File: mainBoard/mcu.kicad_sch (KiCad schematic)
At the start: 25 parts, among them SW2 SW_SPDT, SW3 SW_Push, SW4 SW_Push, U4 STM32F401RETx, Y1 ATS240C-E

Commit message: Nearly finished with board after revisions
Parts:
- added TP17, TP18: TestPoint_Small, TestPoint:TestPoint_Pad_D1.0mm, symbol Connector:TestPoint_Small
- C14, C17, C20, C21, C22, C23, C24: Type (none) -> 50V X7R
- C15, C16: Type (none) -> 6.3V C0G; part number (none) -> 0402N200J500CT
- C18: value 2.2uF Low ESR -> 2.2uF; Type (none) -> 25V X7R; part number (none) -> CL21B225KAFNNNE
- C19: Type (none) -> 16V X7R
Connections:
- net HSE_IN: now also TP17.1
- net HSE_OUT: now also TP18.1
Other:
- note added: "CL21B225KAFNNNE"
- moved on the sheet: C15, C16, C18, C19, D14, D5, R10, R11, R58, R60, R9, SW2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

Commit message: work on AC power side
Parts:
- added TP19, TP20, TP21, TP22, TP23, TP24, TP25, TP26, TP27, TP28, TP29, TP30, TP31: TestPoint_Small, TestPoint:TestPoint_Pad_D1.0mm, symbol Connector:TestPoint_Small
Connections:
- net at U4.10 (PC2): now also TP21.1
- net at U4.11 (PC3): now also TP22.1
- net at U4.2 (PC13): now also TP24.1
- net at U4.21 (PA5): now also TP27.1
- net at U4.25 (PC5): now also TP23.1
- net at U4.26 (PB0): now also TP28.1
- net at U4.27 (PB1): now also TP29.1
- net at U4.28 (PB2): now also TP30.1
- net at U4.29 (PB10): now also TP31.1
- net at U4.3 (PC14): now also TP25.1
- net at U4.4 (PC15): now also TP26.1
- net at U4.8 (PC0): now also TP19.1
- net at U4.9 (PC1): now also TP20.1
- no-connect marks 13 -> 0

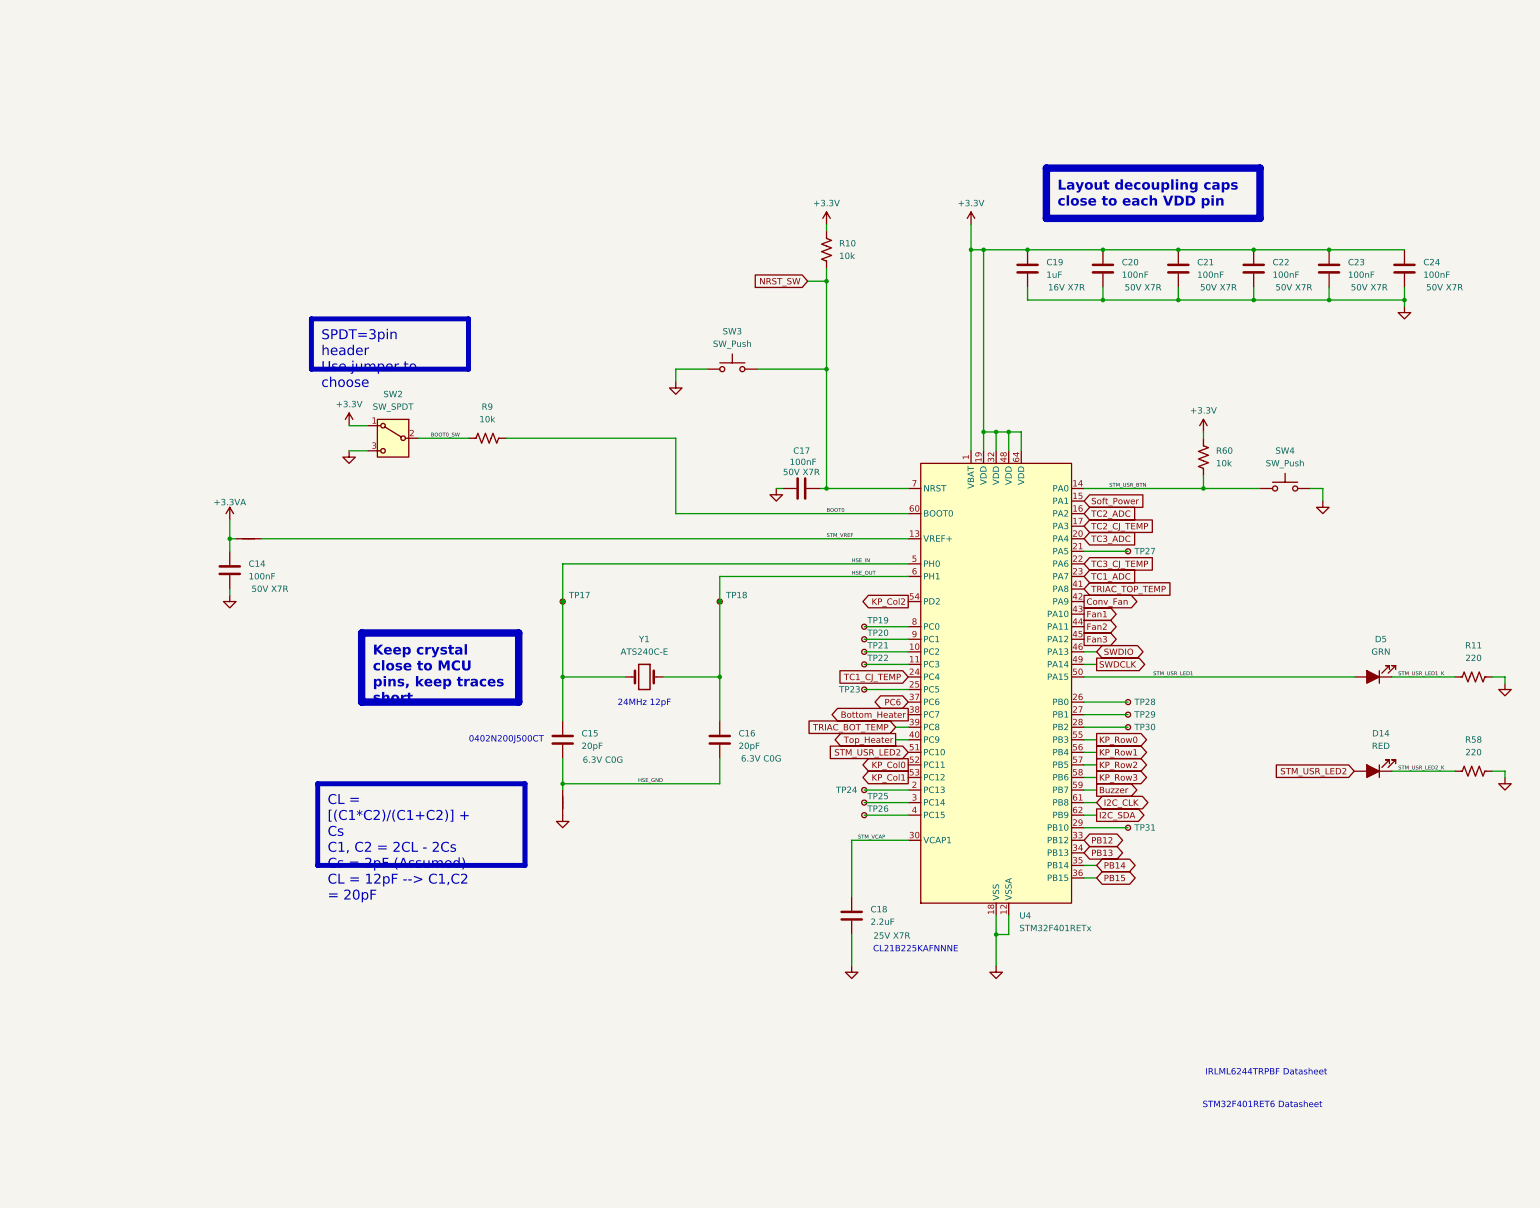
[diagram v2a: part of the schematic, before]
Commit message: add USB-A and change capacitors
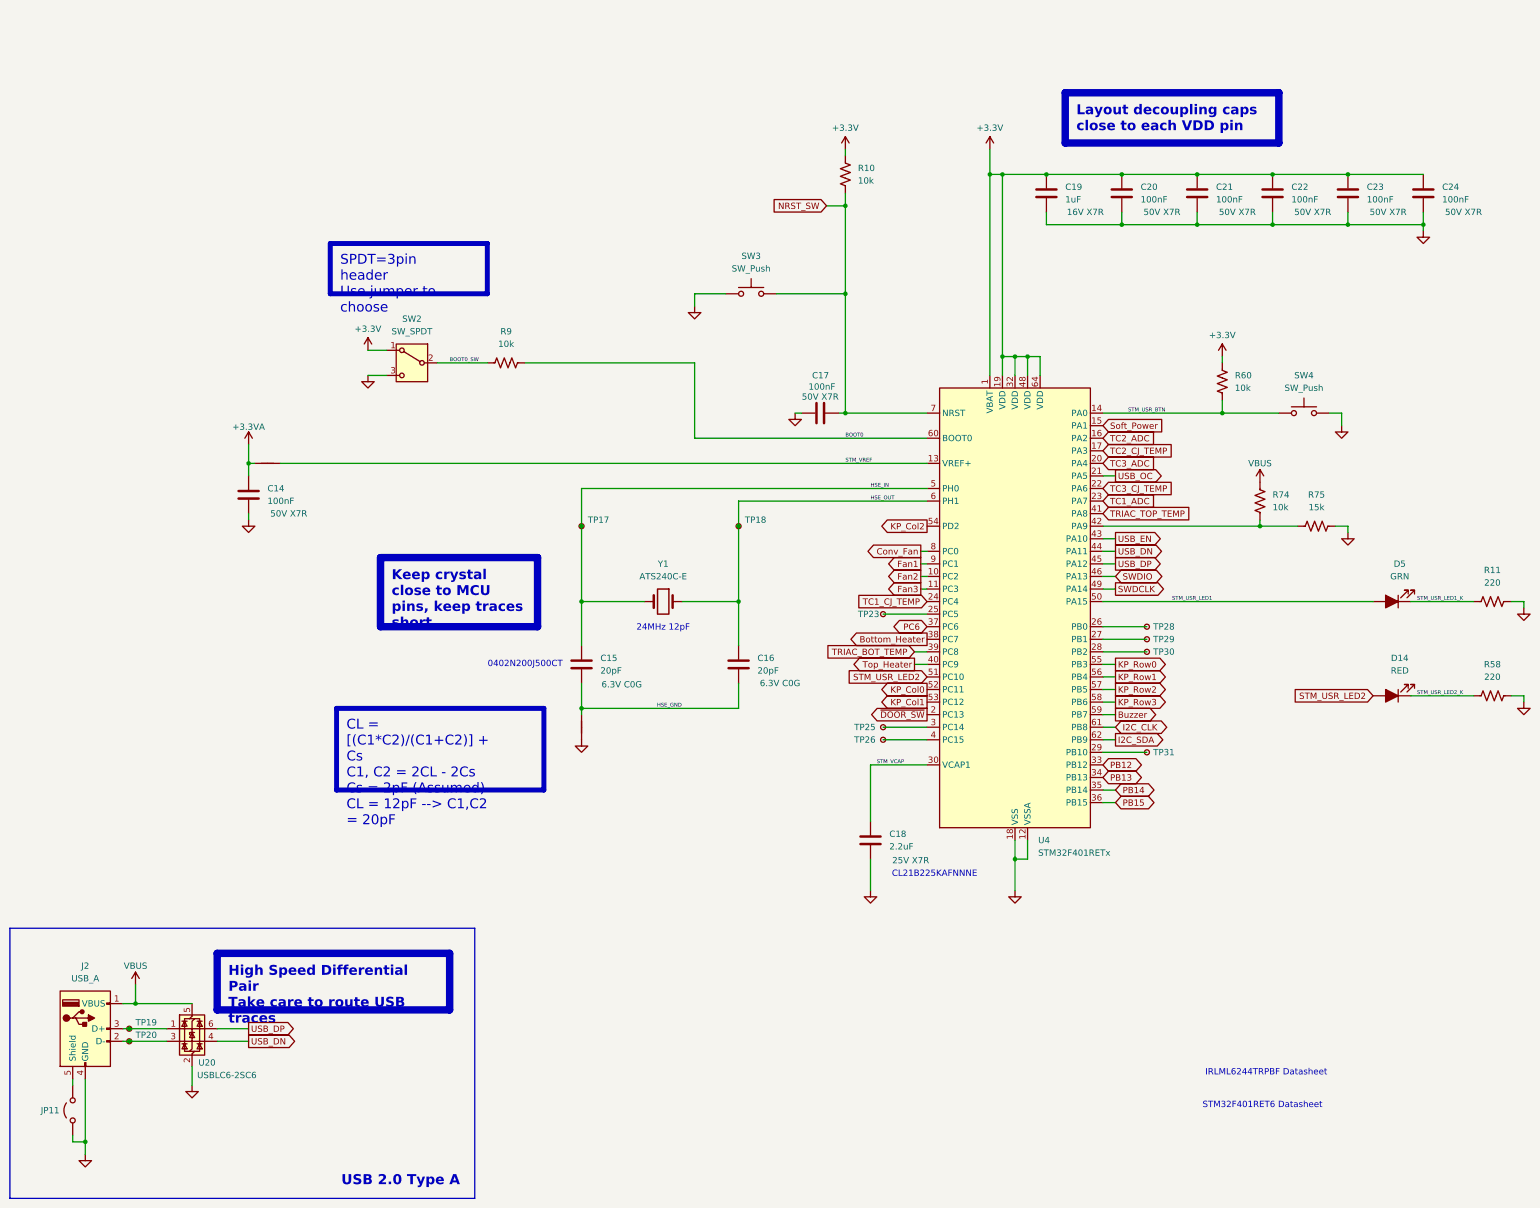
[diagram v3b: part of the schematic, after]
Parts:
- removed TP21, TP22, TP24, TP27: TestPoint_Small, TestPoint:TestPoint_Pad_D1.0mm, symbol Connector:TestPoint_Small
- added J2: USB_A, Connector_USB:USB_A_Connfly_DS1095, symbol Connector:USB_A
- added JP11: Jumper_2_Open, Jumper:SolderJumper-2_P1.3mm_Open_TrianglePad1.0x1.5mm, symbol Jumper:Jumper_2_Open
- added R74: 10k, Resistor_SMD:R_0603_1608Metric_Pad0.98x0.95mm_HandSolder, symbol Device:R_US
- added R75: 15k, Resistor_SMD:R_0603_1608Metric_Pad0.98x0.95mm_HandSolder, symbol Device:R_US
- added U20: USBLC6-2SC6, Package_TO_SOT_SMD:SOT-23-6, symbol Power_Protection:USBLC6-2SC6
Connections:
- net Conv_Fan: now also U4.8 (PC0); no longer U4.42 (PA9)
- net Fan1: now also U4.9 (PC1); no longer U4.43 (PA10)
- net Fan2: now also U4.10 (PC2); no longer U4.44 (PA11)
- net Fan3: now also U4.11 (PC3); no longer U4.45 (PA12)
- net GND: now also J2.4 (GND), JP11.1 (A), R75.2, U20.2 (GND)
- net at TP19.1: now also J2.3 (D+), U20.1 (I/O1); no longer U4.8 (PC0)
- net USB_OC: now reaches U4.21 (PA5)
- net ~{DOOR_SW}: now reaches U4.2 (PC13)
- net at TP20.1: now also J2.2 (D-), U20.3 (I/O2); no longer U4.9 (PC1)
- new net: R74.1, R75.1, U4.42 (PA9)
- new net: J2.5 (Shield), JP11.2 (B)
- new net USB_DN: U20.4 (I/O2), U4.44 (PA11)
- new net USB_DP: U20.6 (I/O1), U4.45 (PA12)
- new net USB_EN: U4.43 (PA10)
- new net VBUS: J2.1 (VBUS), R74.2, U20.5 (VBUS)
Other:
- note added: "USB 2.0 Type A"
- moved on the sheet: C14, C15, C16, C17, C18, C19, C20, C21, C22, C23, C24, D14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

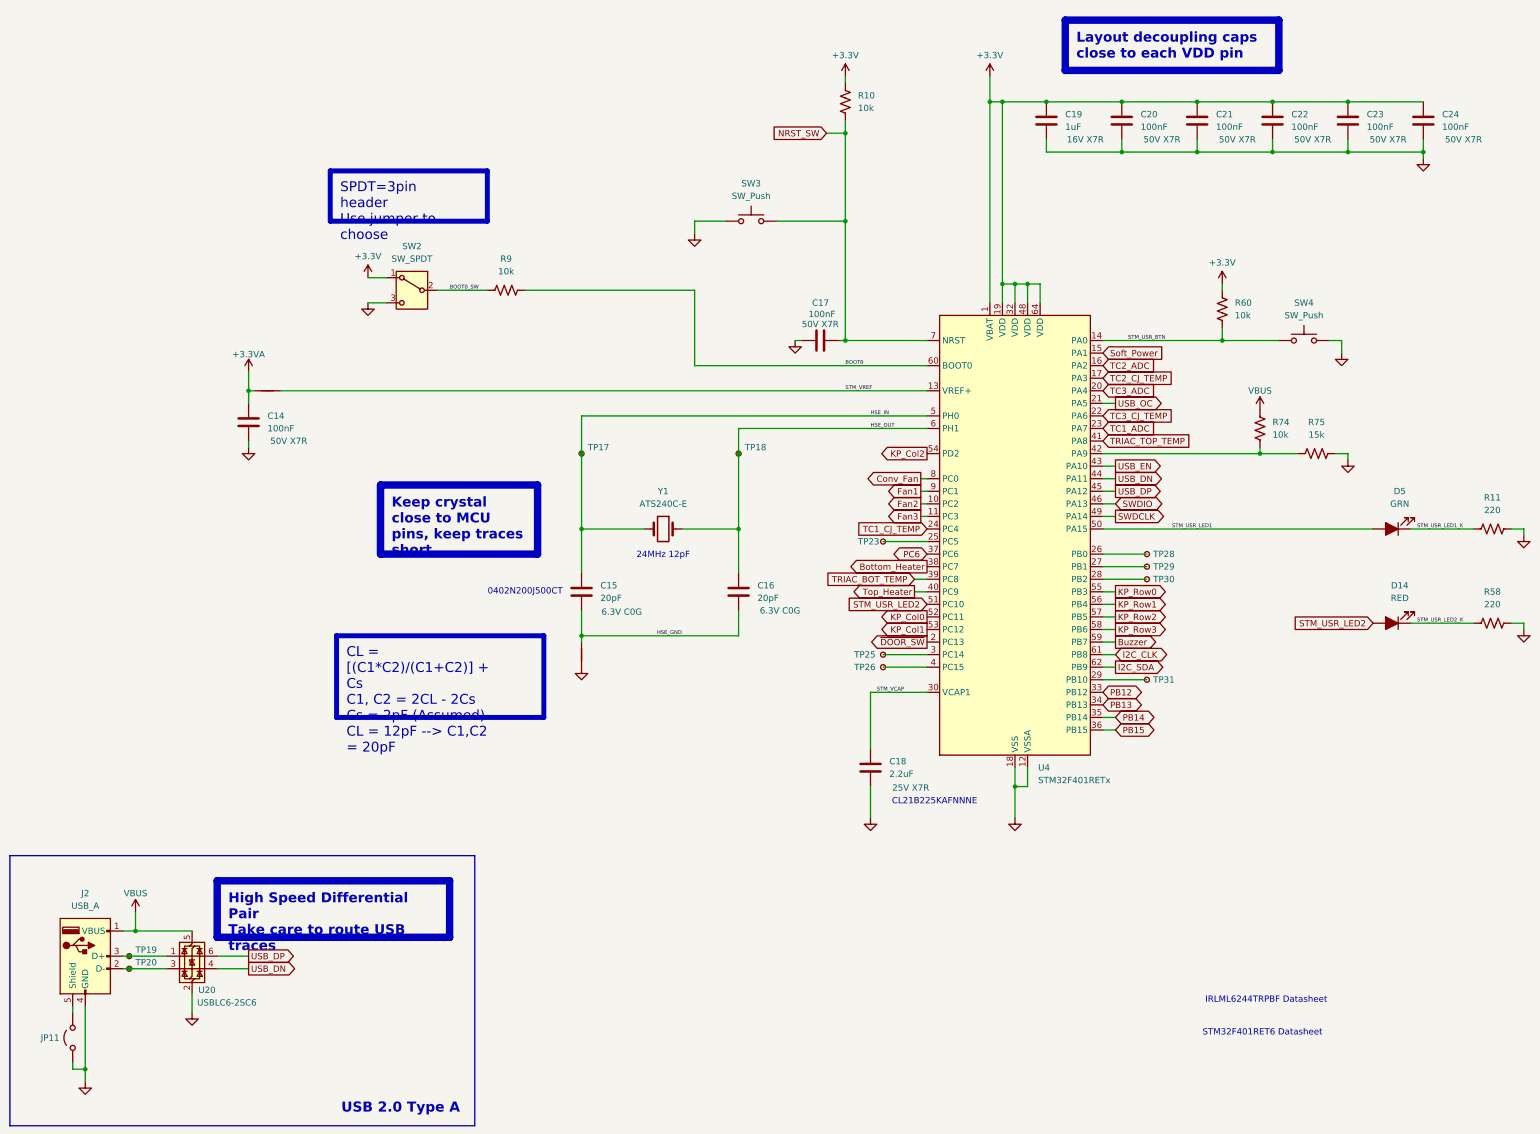
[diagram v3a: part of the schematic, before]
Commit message: change to single 4" touchscreen for UI instead of keypad and buttons
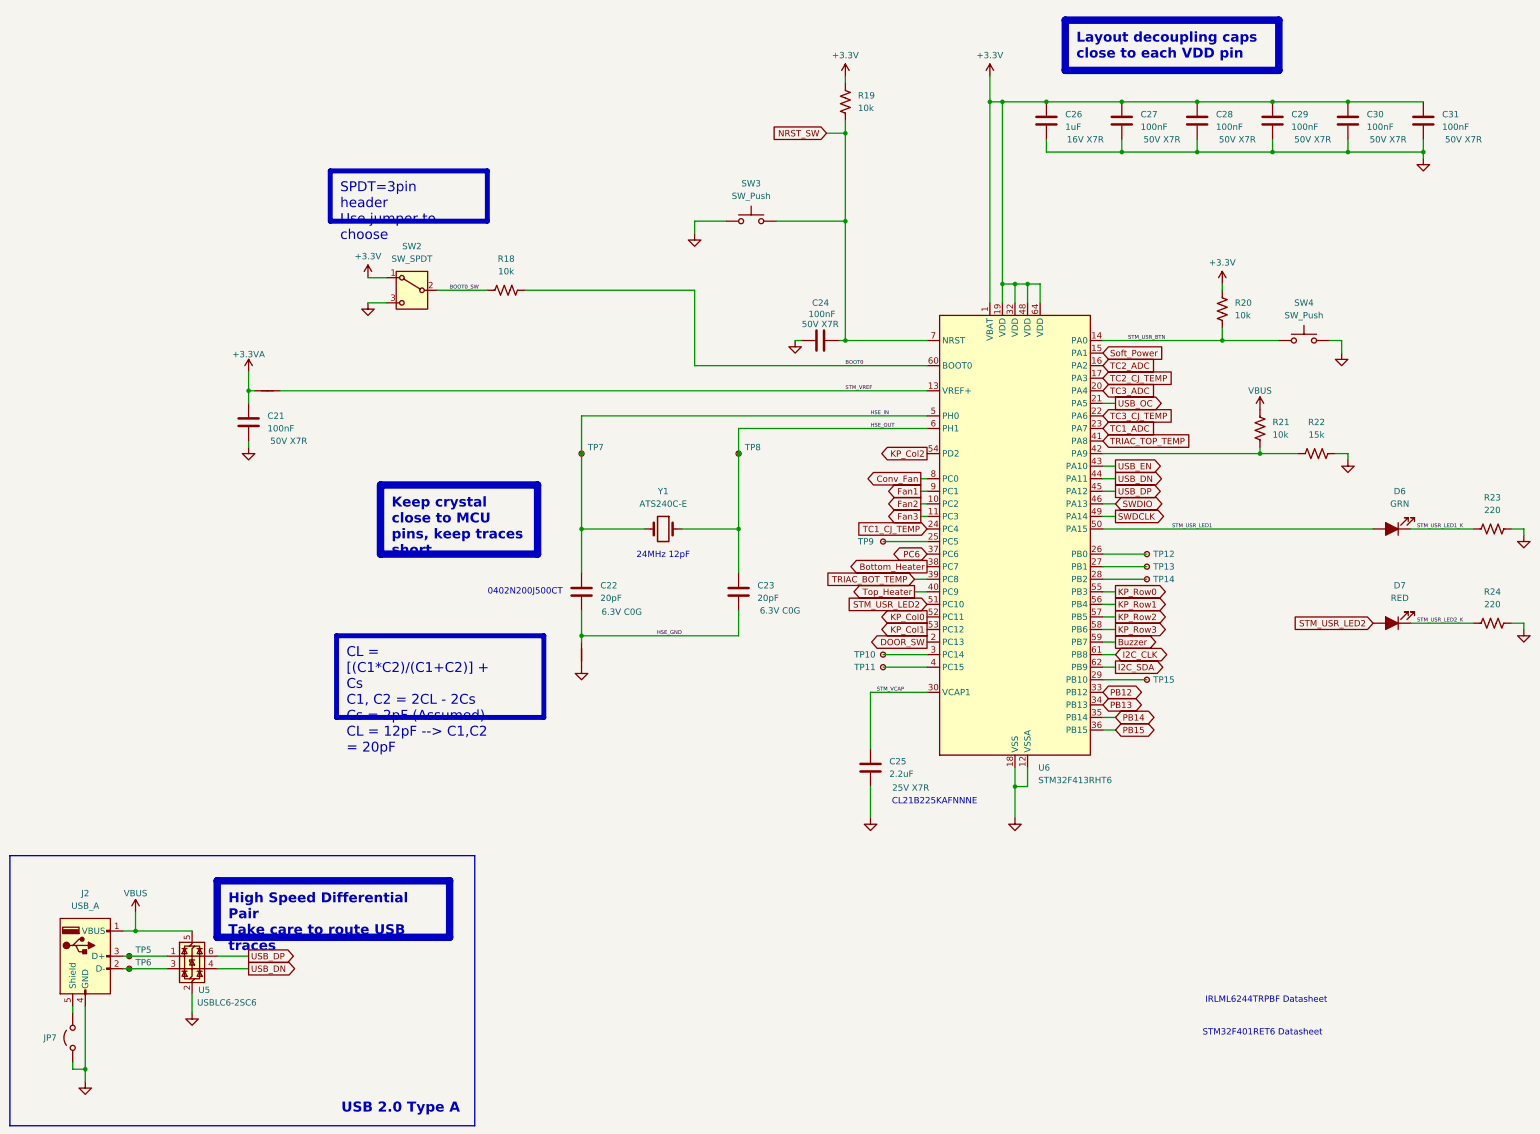
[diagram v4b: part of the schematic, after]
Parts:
- U6: renamed from U4; value STM32F401RETx -> STM32F413RHT6
- renumbered C14 to C21, C15 to C22, C16 to C23, C17 to C24, C18 to C25, C19 to C26, C20 to C27, C21 to C28, C22 to C29, C23 to C30, C24 to C31, D5 to D6, D14 to D7, JP11 to JP7, NT4 to NT1, NT3 to NT2, R9 to R18, R10 to R19, R60 to R20, R74 to R21, R75 to R22, R11 to R23, R58 to R24, TP25 to TP10, TP26 to TP11, TP28 to TP12, TP29 to TP13, TP30 to TP14, TP31 to TP15, TP19 to TP5, TP20 to TP6, TP17 to TP7, TP18 to TP8, TP23 to TP9, U20 to U5
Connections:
- net ~{DOOR_SW} renamed DOOR_SW

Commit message: change to stm32f413 and add a QSPI SRAM
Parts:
- removed TP10, TP11, TP12, TP13, TP14, TP15, TP9: TestPoint_Small, TestPoint:TestPoint_Pad_D1.0mm, symbol Connector:TestPoint_Small
- added C46: 100nF, Capacitor_SMD:C_0603_1608Metric_Pad1.08x0.95mm_HandSolder, symbol Device:C
- added U19: 23LC1024-I/ST, Package_SO:TSSOP-8_4.4x3mm_P0.65mm, symbol MicrochipMemory:24LC1024
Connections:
- net +3.3V: now also C46.1, U19.8 (VCC)
- net Bottom_Heater: no longer U6.38 (PC7)
- net Conv_Fan: no longer U6.8 (PC0)
- net DOOR_SW: no longer U6.2 (PC13)
- net Fan1: no longer U6.9 (PC1)
- net Fan2: no longer U6.10 (PC2)
- net Fan3: no longer U6.11 (PC3)
- net GND: now also C46.2, U19.4 (GND)
- net PB12: no longer U6.33 (PB12)
- net PB13: no longer U6.34 (PB13)
- net PB14: no longer U6.35 (PB14)
- net PB15: no longer U6.36 (PB15)
- net PC6: no longer U6.37 (PC6)
- net STM_USR_BTN: no longer U6.14 (PA0)
- net STM_USR_LED1: no longer U6.50 (PA15)
- net STM_USR_LED2: no longer U6.51 (PC10)
- net Soft_Power: no longer U6.15 (PA1)
- net TC1_ADC: now also U6.22 (PA6); no longer U6.23 (PA7)
- net TC1_CJ_TEMP: no longer U6.24 (PC4)
- net TC2_ADC: now also U6.23 (PA7); no longer U6.16 (PA2)
- net TC2_CJ_TEMP: no longer U6.17 (PA3)
- net TC3_ADC: now also U6.26 (PB0); no longer U6.20 (PA4)
- net TC3_CJ_TEMP: no longer U6.22 (PA6)
- net TRIAC_BOT_TEMP: no longer U6.39 (PC8)
- net TRIAC_TOP_TEMP: no longer U6.41 (PA8)
- net Top_Heater: no longer U6.40 (PC9)
- net USB_EN: no longer U6.43 (PA10)
- net USB_OC: no longer U6.21 (PA5)
- net QSPI_SCK: now reaches U6.27 (PB1)
- net QSPI_SCK: now also U19.6 (SCK)
- net Buzzer: no longer names the net of U6.59 (PB7)
- net I2C_CLK: no longer names the net of U6.61 (PB8)
- net I2C_SDA: no longer names the net of U6.62 (PB9)
- net KP_Col0: no longer names the net of U6.52 (PC11)
- net KP_Col1: no longer names the net of U6.53 (PC12)
- net KP_Col2: no longer names the net of U6.54 (PD2)
- net KP_Row0 renamed SPI1_SCK
- net KP_Row1 renamed SPI1_MISO
- net KP_Row2 renamed SPI1_MOSI
- net KP_Row3 renamed QSPI_SRAM_CS
- net QSPI_SRAM_CS: now also U19.1 (~{CS})
- new net QSPI_SIO0: U19.5 (SI/SIO0), U6.40 (PC9)
- new net QSPI_SIO1: U19.2 (SO/SIO1), U6.51 (PC10)
- new net QSPI_SIO2: U19.3 (SIO2), U6.39 (PC8)
- new net QSPI_SIO3: U19.7 (~{HOLD}/SIO3), U6.15 (PA1)
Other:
- note added: "128 kB QSPI SRAM"
- note added: "STM32 Debugging"
- moved on the sheet: C21, C22, C23, C24, C25, C26, C27, C28, C29, C30, C31, D6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
